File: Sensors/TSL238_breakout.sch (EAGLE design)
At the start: 1 part

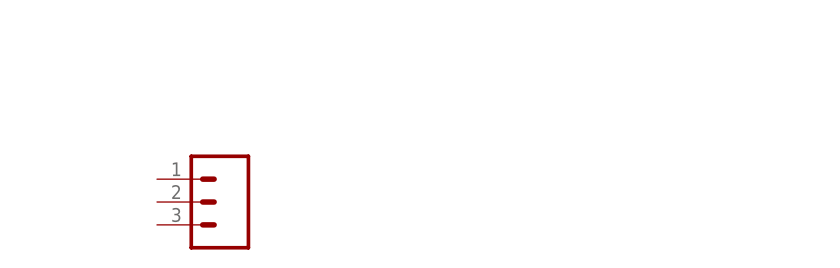
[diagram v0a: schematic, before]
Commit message: Updated TSL238
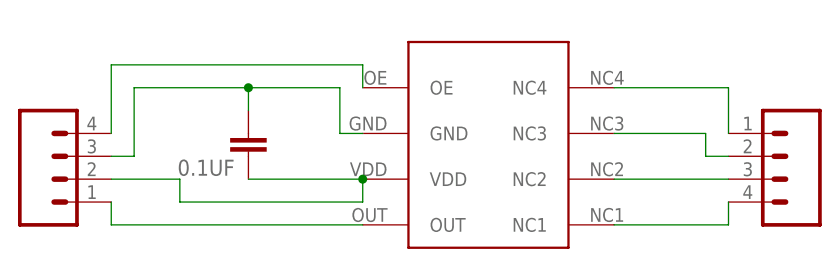
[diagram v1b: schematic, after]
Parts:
- added 0.1UF: (no value), SparkFun-Capacitors:CAP0603-CAP
- added J2: (no value), SparkFun-Connectors:M04PTH
- added U$1: TSL238, awqua_eagle_library:TSL238
- J1: device SparkFun-Connectors:M03PTH -> SparkFun-Connectors:M04PTH
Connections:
- new net N$1: J2.1, U$1.NC4
- new net N$2: J2.2, U$1.NC3
- new net N$3: J2.3, U$1.NC2
- new net N$4: J2.4, U$1.NC1
- new net N$5: J1.4, U$1.OE
- new net N$6: 0.1UF.1, J1.2, U$1.VDD
- new net N$8: J1.1, U$1.OUT
- new net N$9: 0.1UF.2, J1.3, U$1.GND
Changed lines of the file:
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@@
 <layer number="19" name="Unrouted" color="6" fill="1" visible="no" active="no"/>
 <layer number="20" name="Dimension" color="15" fill="1" visible="no" active="no"/>
-<layer number="21" name="tPlace" color="16" fill="1" visible="no" active="no"/>
+<layer number="21" name="tPlace" color="7" fill="1" visible="no" active="no"/>
 <layer number="22" name="bPlace" color="7" fill="1" visible="no" active="no"/>
 <layer number="23" name="tOrigins" color="15" fill="1" visible="no" active="no"/>
@@
 <layer number="49" name="Reference" color="7" fill="1" visible="no" active="no"/>
 <layer number="50" name="dxf" color="7" fill="1" visible="no" active="no"/>
-<layer number="51" name="tDocu" color="14" fill="1" visible="no" active="no"/>
+<layer number="51" name="tDocu" color="7" fill="1" visible="no" active="no"/>
 <layer number="52" name="bDocu" color="7" fill="1" visible="no" active="no"/>
 <layer number="53" name="tGND_GNDA" color="7" fill="9" visible="no" active="no"/>
@@
 <layer number="111" name="LPC17xx" color="7" fill="1" visible="yes" active="yes"/>
 <layer number="112" name="tSilk" color="7" fill="1" visible="yes" active="yes"/>
-<layer number="113" name="IDFDebug" color="4" fill="1" visible="yes" active="yes"/>
+<layer number="113" name="IDFDebug" color="7" fill="1" visible="yes" active="yes"/>
 <layer number="114" name="Badge_Outline" color="7" fill="1" visible="yes" active="yes"/>
 <layer number="115" name="ReferenceISLANDS" color="7" fill="1" visible="yes" active="yes"/>
@@
 </classes>
 <parts>
-<part name="J1" library="SparkFun-Connectors" deviceset="M03" device="PTH"/>
+<part name="U$1" library="awqua_eagle_library" deviceset="TSL238" device=""/>
+<part name="0.1UF" library="SparkFun-Capacitors" deviceset="CAP" device="0603-CAP"/>
+<part name="J1" library="SparkFun-Connectors" deviceset="M04" device="PTH"/>
+<part name="J2" library="SparkFun-Connectors" deviceset="M04" device="PTH"/>
 </parts>
 <sheets>
@@
 </plain>
 <instances>
-<instance part="J1" gate="J$1" x="25.4" y="7.62" smashed="yes" rot="R180">
-<attribute name="VALUE" x="27.94" y="15.24" size="1.778" layer="96" rot="R180"/>
+<instance part="U$1" gate="G$1" x="55.88" y="12.7" rot="R90"/>
+<instance part="0.1UF" gate="G$1" x="27.94" y="15.24" rot="R180"/>
+<instance part="J1" gate="G$1" x="7.62" y="10.16" smashed="yes">
+<attribute name="VALUE" x="2.54" y="2.54" size="1.778" layer="96"/>
+</instance>
+<instance part="J2" gate="G$1" x="86.36" y="12.7" smashed="yes" rot="R180">
+<attribute name="VALUE" x="91.44" y="20.32" size="1.778" layer="96" rot="R180"/>
 </instance>
 </instances>
@@
 </busses>
 <nets>
+<net name="N$1" class="0">
+<segment>
+<pinref part="U$1" gate="G$1" pin="NC4"/>
+<pinref part="J2" gate="G$1" pin="1"/>
+<wire x1="68.58" y1="20.32" x2="81.28" y2="20.32" width="0.1524" layer="91"/>
+<wire x1="81.28" y1="20.32" x2="81.28" y2="15.24" width="0.1524" layer="91"/>
+</segment>
+</net>
+<net name="N$2" class="0">
+<segment>
+<pinref part="U$1" gate="G$1" pin="NC3"/>
+<wire x1="68.58" y1="15.24" x2="78.74" y2="15.24" width="0.1524" layer="91"/>
+<wire x1="78.74" y1="15.24" x2="78.74" y2="12.7" width="0.1524" layer="91"/>
+<pinref part="J2" gate="G$1" pin="2"/>
+<wire x1="78.74" y1="12.7" x2="81.28" y2="12.7" width="0.1524" layer="91"/>
+</segment>
+</net>
+<net name="N$3" class="0">
+<segment>
+<pinref part="U$1" gate="G$1" pin="NC2"/>
+<pinref part="J2" gate="G$1" pin="3"/>
+<wire x1="68.58" y1="10.16" x2="81.28" y2="10.16" width="0.1524" layer="91"/>
+</segment>
+</net>
+<net name="N$4" class="0">
+<segment>
+<pinref part="U$1" gate="G$1" pin="NC1"/>
+<pinref part="J2" gate="G$1" pin="4"/>
+<wire x1="68.58" y1="5.08" x2="81.28" y2="5.08" width="0.1524" layer="91"/>
+<wire x1="81.28" y1="5.08" x2="81.28" y2="7.62" width="0.1524" layer="91"/>
+</segment>
+</net>
+<net name="N$5" class="0">
+<segment>
+<pinref part="U$1" gate="G$1" pin="OE"/>
+<wire x1="40.64" y1="20.32" x2="40.64" y2="22.86" width="0.1524" layer="91"/>
+<pinref part="J1" gate="G$1" pin="4"/>
+<wire x1="40.64" y1="22.86" x2="12.7" y2="22.86" width="0.1524" layer="91"/>
+<wire x1="12.7" y1="22.86" x2="12.7" y2="15.24" width="0.1524" layer="91"/>
+</segment>
+</net>
+<net name="N$8" class="0">
+<segment>
+<pinref part="U$1" gate="G$1" pin="OUT"/>
+<pinref part="J1" gate="G$1" pin="1"/>
+<wire x1="40.64" y1="5.08" x2="12.7" y2="5.08" width="0.1524" layer="91"/>
+<wire x1="12.7" y1="5.08" x2="12.7" y2="7.62" width="0.1524" layer="91"/>
+</segment>
+</net>
+<net name="N$9" class="0">
+<segment>
+<wire x1="15.24" y1="20.32" x2="15.24" y2="12.7" width="0.1524" layer="91"/>
+<pinref part="J1" gate="G$1" pin="3"/>
+<wire x1="15.24" y1="12.7" x2="12.7" y2="12.7" width="0.1524" layer="91"/>
+<wire x1="15.24" y1="20.32" x2="27.94" y2="20.32" width="0.1524" layer="91"/>
+<wire x1="27.94" y1="20.32" x2="38.1" y2="20.32" width="0.1524" layer="91"/>
+<wire x1="38.1" y1="20.32" x2="38.1" y2="15.24" width="0.1524" layer="91"/>
+<pinref part="U$1" gate="G$1" pin="GND"/>
+<wire x1="38.1" y1="15.24" x2="40.64" y2="15.24" width="0.1524" layer="91"/>
+<pinref part="0.1UF" gate="G$1" pin="2"/>
+<wire x1="27.94" y1="17.78" x2="27.94" y2="20.32" width="0.1524" layer="91"/>
+<junction x="27.94" y="20.32"/>
+</segment>
+</net>
+<net name="N$6" class="0">
+<segment>
+<pinref part="J1" gate="G$1" pin="2"/>
+<wire x1="20.32" y1="10.16" x2="12.7" y2="10.16" width="0.1524" layer="91"/>
+<wire x1="20.32" y1="10.16" x2="20.32" y2="7.62" width="0.1524" layer="91"/>
+<pinref part="0.1UF" gate="G$1" pin="1"/>
+<pinref part="U$1" gate="G$1" pin="VDD"/>
+<wire x1="40.64" y1="10.16" x2="27.94" y2="10.16" width="0.1524" layer="91"/>
+<wire x1="20.32" y1="7.62" x2="40.64" y2="7.62" width="0.1524" layer="91"/>
+<wire x1="40.64" y1="7.62" x2="40.64" y2="10.16" width="0.1524" layer="91"/>
+<junction x="40.64" y="10.16"/>
+</segment>
+</net>
 </nets>
 </sheet>

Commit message: updated tsl238
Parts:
- removed J2: (no value), SparkFun-Connectors:M04PTH
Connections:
- net N$5 renamed OE
- net N$6 renamed VCC
- net N$8 renamed OUT
- net N$9 renamed GND
- removed net N$1: J2.1, U$1.NC4
- removed net N$2: J2.2, U$1.NC3
- removed net N$3: J2.3, U$1.NC2
- removed net N$4: J2.4, U$1.NC1
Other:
- moved on the sheet: 0.1UF
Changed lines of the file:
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@@
 <?xml version="1.0" encoding="utf-8"?>
 <!DOCTYPE eagle SYSTEM "eagle.dtd">
-<eagle version="7.3.0">
+<eagle version="7.7.0">
 <drawing>
 <settings>
@@
 <part name="0.1UF" library="SparkFun-Capacitors" deviceset="CAP" device="0603-CAP"/>
 <part name="J1" library="SparkFun-Connectors" deviceset="M04" device="PTH"/>
-<part name="J2" library="SparkFun-Connectors" deviceset="M04" device="PTH"/>
 </parts>
 <sheets>
@@
 </plain>
 <instances>
-<instance part="U$1" gate="G$1" x="55.88" y="12.7" rot="R90"/>
-<instance part="0.1UF" gate="G$1" x="27.94" y="15.24" rot="R180"/>
-<instance part="J1" gate="G$1" x="7.62" y="10.16" smashed="yes">
-<attribute name="VALUE" x="2.54" y="2.54" size="1.778" layer="96"/>
-</instance>
-<instance part="J2" gate="G$1" x="86.36" y="12.7" smashed="yes" rot="R180">
-<attribute name="VALUE" x="91.44" y="20.32" size="1.778" layer="96" rot="R180"/>
+<instance part="U$1" gate="G$1" x="38.1" y="17.78" rot="R270"/>
+<instance part="0.1UF" gate="G$1" x="66.04" y="15.24"/>
+<instance part="J1" gate="G$1" x="86.36" y="20.32" smashed="yes" rot="R180">
+<attribute name="VALUE" x="91.44" y="27.94" size="1.778" layer="96" rot="R180"/>
 </instance>
 </instances>
@@
 </busses>
 <nets>
-<net name="N$1" class="0">
-<segment>
-<pinref part="U$1" gate="G$1" pin="NC4"/>
-<pinref part="J2" gate="G$1" pin="1"/>
-<wire x1="68.58" y1="20.32" x2="81.28" y2="20.32" width="0.1524" layer="91"/>
-<wire x1="81.28" y1="20.32" x2="81.28" y2="15.24" width="0.1524" layer="91"/>
-</segment>
-</net>
-<net name="N$2" class="0">
-<segment>
-<pinref part="U$1" gate="G$1" pin="NC3"/>
-<wire x1="68.58" y1="15.24" x2="78.74" y2="15.24" width="0.1524" layer="91"/>
-<wire x1="78.74" y1="15.24" x2="78.74" y2="12.7" width="0.1524" layer="91"/>
-<pinref part="J2" gate="G$1" pin="2"/>
-<wire x1="78.74" y1="12.7" x2="81.28" y2="12.7" width="0.1524" layer="91"/>
-</segment>
-</net>
-<net name="N$3" class="0">
-<segment>
-<pinref part="U$1" gate="G$1" pin="NC2"/>
-<pinref part="J2" gate="G$1" pin="3"/>
-<wire x1="68.58" y1="10.16" x2="81.28" y2="10.16" width="0.1524" layer="91"/>
-</segment>
-</net>
-<net name="N$4" class="0">
-<segment>
-<pinref part="U$1" gate="G$1" pin="NC1"/>
-<pinref part="J2" gate="G$1" pin="4"/>
-<wire x1="68.58" y1="5.08" x2="81.28" y2="5.08" width="0.1524" layer="91"/>
-<wire x1="81.28" y1="5.08" x2="81.28" y2="7.62" width="0.1524" layer="91"/>
-</segment>
-</net>
-<net name="N$5" class="0">
+<net name="OE" class="0">
 <segment>
 <pinref part="U$1" gate="G$1" pin="OE"/>
-<wire x1="40.64" y1="20.32" x2="40.64" y2="22.86" width="0.1524" layer="91"/>
+<wire x1="53.34" y1="10.16" x2="53.34" y2="7.62" width="0.1524" layer="91"/>
 <pinref part="J1" gate="G$1" pin="4"/>
-<wire x1="40.64" y1="22.86" x2="12.7" y2="22.86" width="0.1524" layer="91"/>
-<wire x1="12.7" y1="22.86" x2="12.7" y2="15.24" width="0.1524" layer="91"/>
-</segment>
-</net>
-<net name="N$8" class="0">
+<wire x1="53.34" y1="7.62" x2="81.28" y2="7.62" width="0.1524" layer="91"/>
+<wire x1="81.28" y1="7.62" x2="81.28" y2="15.24" width="0.1524" layer="91"/>
+</segment>
+</net>
+<net name="OUT" class="0">
 <segment>
 <pinref part="U$1" gate="G$1" pin="OUT"/>
 <pinref part="J1" gate="G$1" pin="1"/>
-<wire x1="40.64" y1="5.08" x2="12.7" y2="5.08" width="0.1524" layer="91"/>
-<wire x1="12.7" y1="5.08" x2="12.7" y2="7.62" width="0.1524" layer="91"/>
-</segment>
-</net>
-<net name="N$9" class="0">
-<segment>
-<wire x1="15.24" y1="20.32" x2="15.24" y2="12.7" width="0.1524" layer="91"/>
+<wire x1="53.34" y1="25.4" x2="81.28" y2="25.4" width="0.1524" layer="91"/>
+<wire x1="81.28" y1="25.4" x2="81.28" y2="22.86" width="0.1524" layer="91"/>
+</segment>
+</net>
+<net name="GND" class="0">
+<segment>
+<wire x1="78.74" y1="10.16" x2="78.74" y2="17.78" width="0.1524" layer="91"/>
 <pinref part="J1" gate="G$1" pin="3"/>
-<wire x1="15.24" y1="12.7" x2="12.7" y2="12.7" width="0.1524" layer="91"/>
-<wire x1="15.24" y1="20.32" x2="27.94" y2="20.32" width="0.1524" layer="91"/>
-<wire x1="27.94" y1="20.32" x2="38.1" y2="20.32" width="0.1524" layer="91"/>
-<wire x1="38.1" y1="20.32" x2="38.1" y2="15.24" width="0.1524" layer="91"/>
+<wire x1="78.74" y1="17.78" x2="81.28" y2="17.78" width="0.1524" layer="91"/>
+<wire x1="78.74" y1="10.16" x2="66.04" y2="10.16" width="0.1524" layer="91"/>
+<wire x1="66.04" y1="10.16" x2="55.88" y2="10.16" width="0.1524" layer="91"/>
+<wire x1="55.88" y1="10.16" x2="55.88" y2="15.24" width="0.1524" layer="91"/>
 <pinref part="U$1" gate="G$1" pin="GND"/>
-<wire x1="38.1" y1="15.24" x2="40.64" y2="15.24" width="0.1524" layer="91"/>
+<wire x1="55.88" y1="15.24" x2="53.34" y2="15.24" width="0.1524" layer="91"/>
 <pinref part="0.1UF" gate="G$1" pin="2"/>
-<wire x1="27.94" y1="17.78" x2="27.94" y2="20.32" width="0.1524" layer="91"/>
-<junction x="27.94" y="20.32"/>
-</segment>
-</net>
-<net name="N$6" class="0">
+<wire x1="66.04" y1="12.7" x2="66.04" y2="10.16" width="0.1524" layer="91"/>
+<junction x="66.04" y="10.16"/>
+</segment>
+</net>
+<net name="VCC" class="0">
 <segment>
 <pinref part="J1" gate="G$1" pin="2"/>
-<wire x1="20.32" y1="10.16" x2="12.7" y2="10.16" width="0.1524" layer="91"/>
-<wire x1="20.32" y1="10.16" x2="20.32" y2="7.62" width="0.1524" layer="91"/>
+<wire x1="73.66" y1="20.32" x2="81.28" y2="20.32" width="0.1524" layer="91"/>
+<wire x1="73.66" y1="20.32" x2="73.66" y2="22.86" width="0.1524" layer="91"/>
 <pinref part="0.1UF" gate="G$1" pin="1"/>
 <pinref part="U$1" gate="G$1" pin="VDD"/>
-<wire x1="40.64" y1="10.16" x2="27.94" y2="10.16" width="0.1524" layer="91"/>
-<wire x1="20.32" y1="7.62" x2="40.64" y2="7.62" width="0.1524" layer="91"/>
-<wire x1="40.64" y1="7.62" x2="40.64" y2="10.16" width="0.1524" layer="91"/>
-<junction x="40.64" y="10.16"/>
-</segment>
-</net>
+<wire x1="53.34" y1="20.32" x2="66.04" y2="20.32" width="0.1524" layer="91"/>
+<wire x1="73.66" y1="22.86" x2="53.34" y2="22.86" width="0.1524" layer="91"/>
+<wire x1="53.34" y1="22.86" x2="53.34" y2="20.32" width="0.1524" layer="91"/>
+<junction x="53.34" y="20.32"/>
+</segment>
+</net>
